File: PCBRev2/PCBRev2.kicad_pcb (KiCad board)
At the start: 2 copper layers, 223.5 x 160 mm, 55 parts, among them J1 Conn_02x40_Counter_Clockwise, J3 512964594, J5 Keypad, J6 Conn_02x10_Odd_Even, J7 54-00164, Q1 2N7000, SW1 SW_Push, SW2 SW_Push, SW3 SW_Push, U1 NUCLEO-G0B1RE, U10 BH1750FVI-TR, U11 MCP6002-I_P, U12 DRV8833PWP, U2 LP-MSPM0G3507, U4 SN74AHC14N, U5 LM7805_TO220, U6 TLV1117-33, U7 COM-09032, U8 WST-1205S, U9 AL5809-20QP1-7

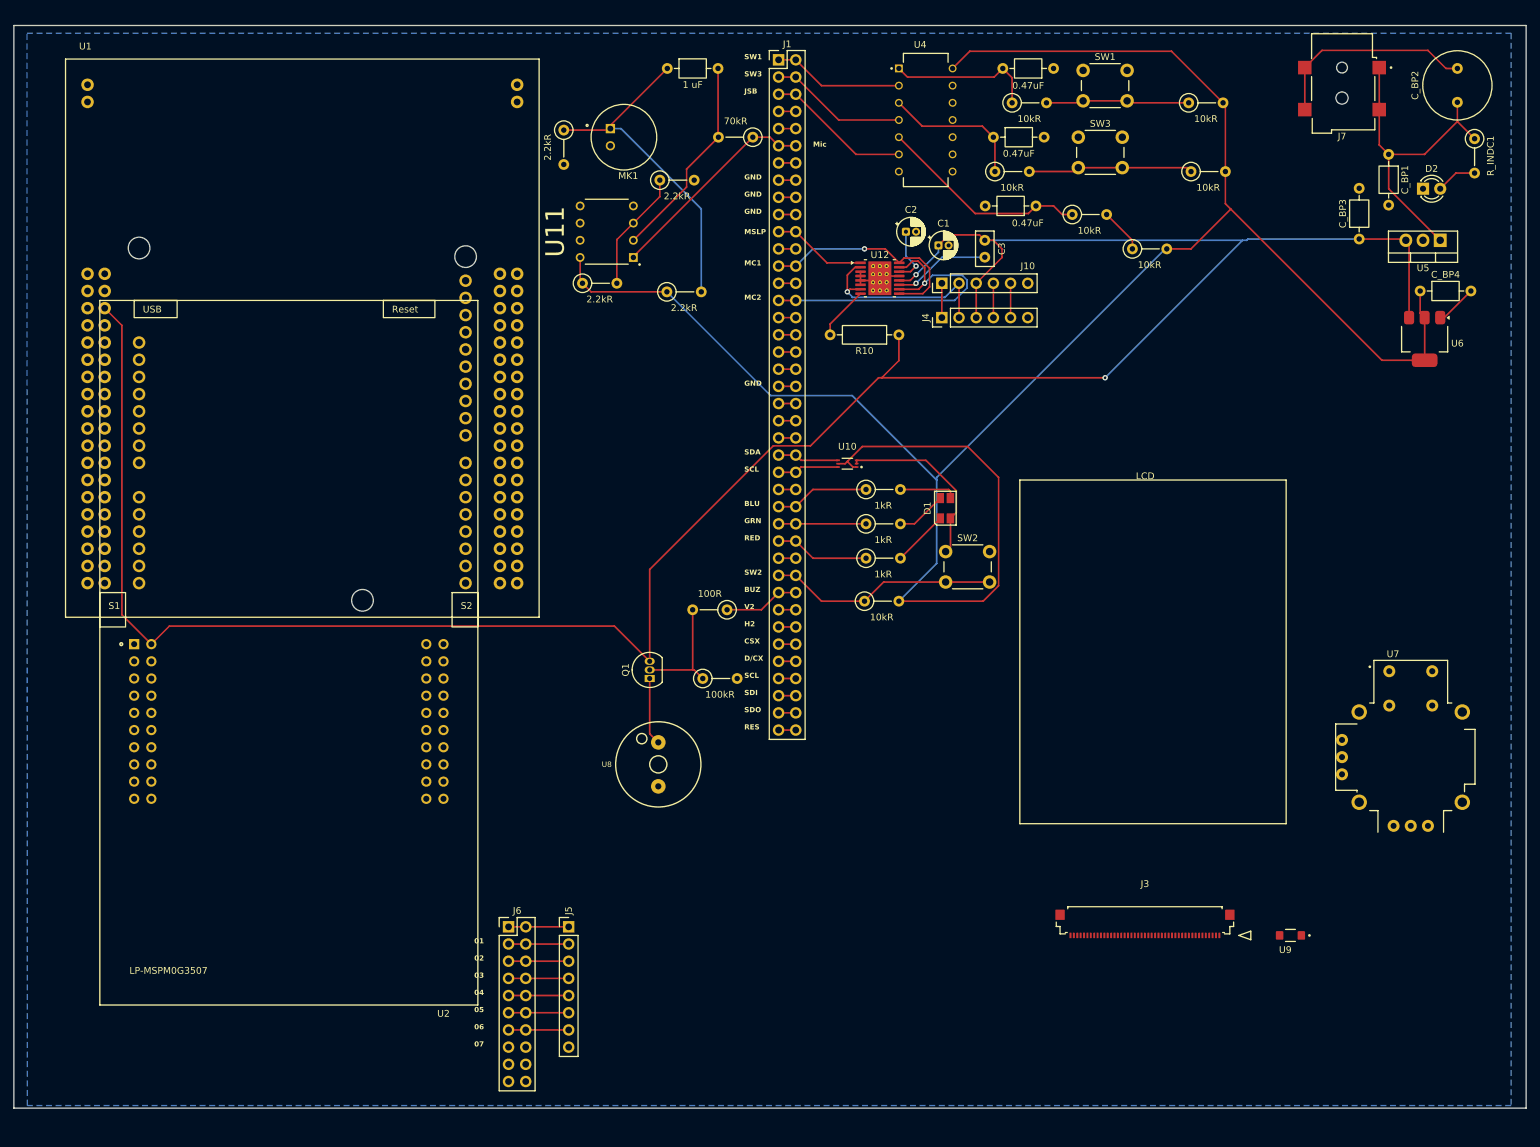
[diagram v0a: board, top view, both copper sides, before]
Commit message: Routing for second revision of the PCB
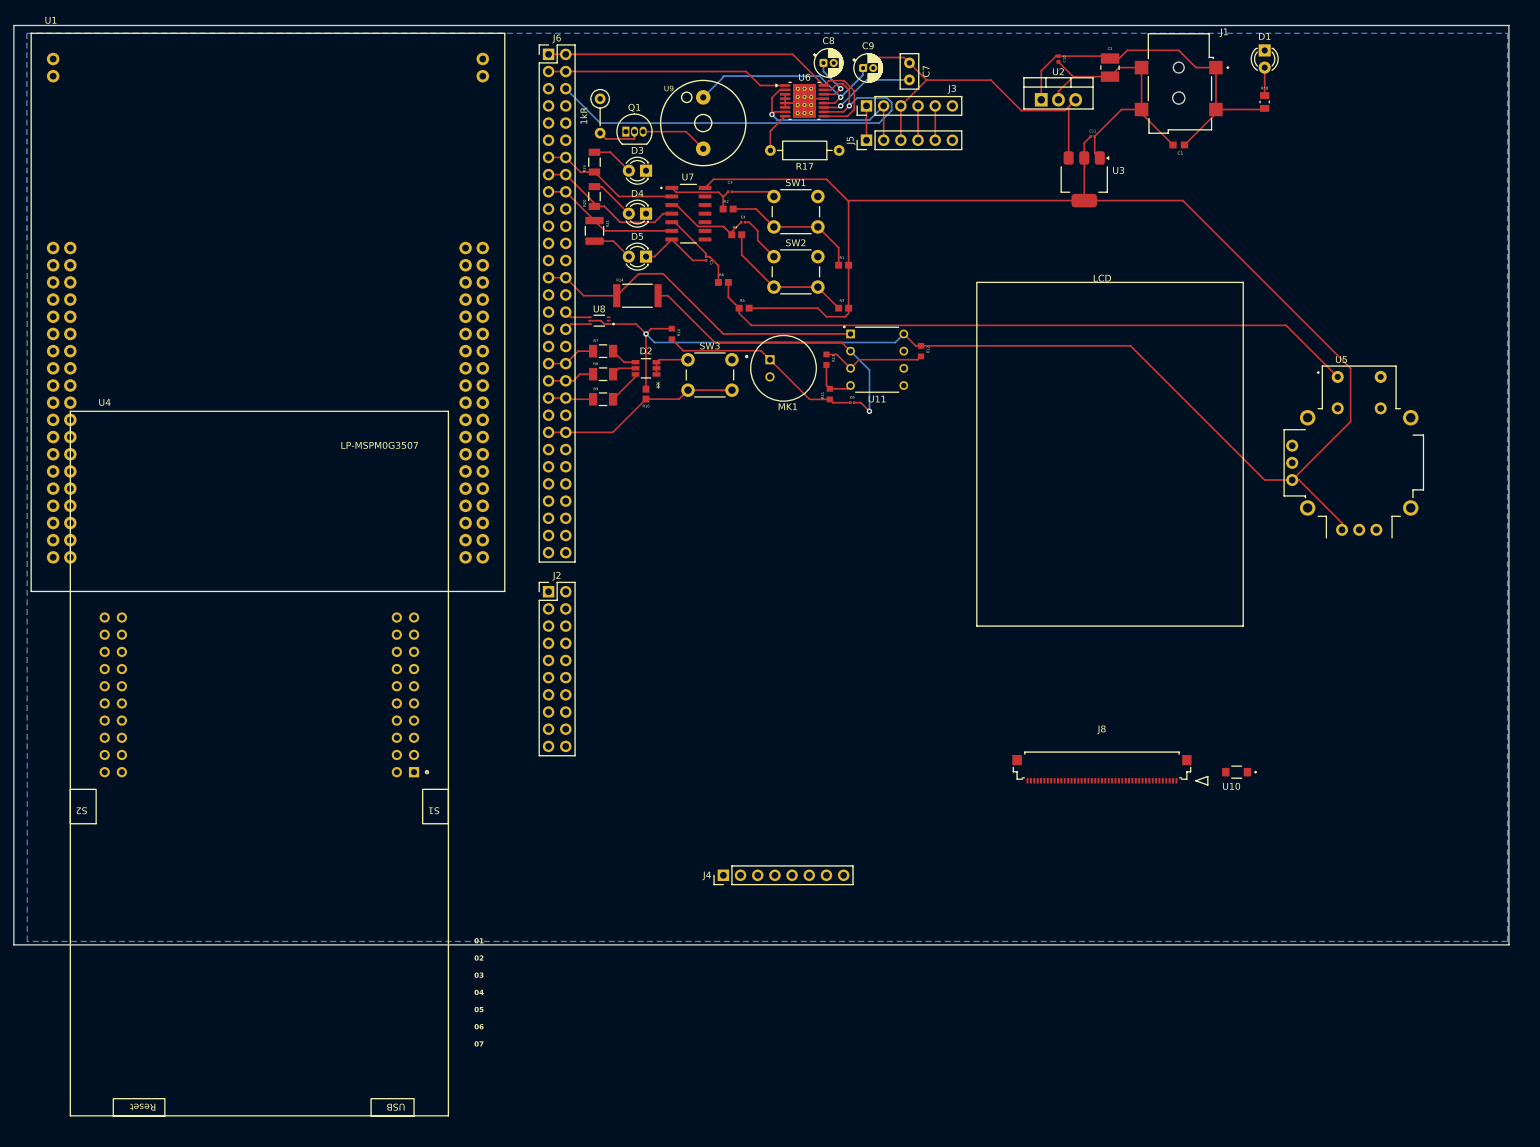
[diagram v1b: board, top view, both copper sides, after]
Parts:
- removed C_BP3, C_BP4: 100 uf, Capacitor_THT:C_Axial_L3.8mm_D2.6mm_P7.50mm_Horizontal
- removed the D1 at (148.4, 82.9)
- removed the J1 at (123.7, 16.6)
- removed R_BUZ2: 100kR, Resistor_THT:R_Axial_DIN0207_L6.3mm_D2.5mm_P5.08mm_Vertical
- removed the U8 at (106.0, 120.8)
- added C10: 0.22uf, GRM155R71C224KA12D022uf.step:CAPC1005X55N, F.Cu at (165.1, 16.5)
- added C11: 1uf, CL03A105KP3NSNC1uf.step:CAPC0603X35N, F.Cu at (170.2, 27.9)
- added D2: AAAF3529LSEEZGKQBKS, footprints:LED_AAAF3529LSEEZGKQBKS_KNB, F.Cu at (104.1, 62.2)
- added D3: LED, LED_THT:LED_D3.0mm_FlatTop, F.Cu at (104.1, 33.0)
- added D4: LED, LED_THT:LED_D3.0mm_FlatTop, F.Cu at (104.1, 39.4)
- added D5: LED, LED_THT:LED_D3.0mm_FlatTop, F.Cu at (104.1, 45.7)
- added J6: Conn_02x30_Odd_Even, Connector_PinHeader_2.54mm:PinHeader_2x30_P2.54mm_Vertical, F.Cu at (89.7, 15.8)
- added R19: 68, CRGCQ1206F68R.step:RESC3115X65N, F.Cu at (96.5, 31.8)
- added R20: 68, CRGCQ1206F68R.step:RESC3115X65N, F.Cu at (96.5, 36.8)
- added R21: 330, CRCW1210330RFKEAHP.step:RESC3225X70N, F.Cu at (96.5, 41.9)
- added U9: WST-1205S, WST-1205S.step:WST-1205S, F.Cu at (112.6, 26.0)
- C1: renamed from C_BP1; value 0.1 uf -> 0.1uf; footprint Capacitor_THT:C_Axial_L3.8mm_D2.6mm_P7.50mm_Horizontal -> C01UF.step:CAPC1608X90
- C2: renamed from C_BP2; value 47 uf -> 47uf; footprint Capacitor_THT:C_Radial_D10.0mm_H20.0mm_P5.00mm -> GRM32EC81C476KE15L.step:CAPC3225X270N
- C3: renamed from CSW1; footprint Capacitor_THT:C_Axial_L3.8mm_D2.6mm_P7.50mm_Horizontal -> GRM033R60J474KE90D.step:CAPC0603X33N
- C4: renamed from CSW3; footprint Capacitor_THT:C_Axial_L3.8mm_D2.6mm_P7.50mm_Horizontal -> GRM033R60J474KE90D.step:CAPC0603X33N
- C5: renamed from CJS1; footprint Capacitor_THT:C_Axial_L3.8mm_D2.6mm_P7.50mm_Horizontal -> GRM033R60J474KE90D.step:CAPC0603X33N
- C6: renamed from C_s2; footprint Capacitor_THT:C_Axial_L3.8mm_D2.6mm_P7.50mm_Horizontal -> CL03A105KP3NSNC1uf.step:CAPC0603X35N
- Q1: value 2N7000 -> 2N4401
- R1: renamed from PullUpResistorSW1; footprint Resistor_THT:R_Axial_DIN0207_L6.3mm_D2.5mm_P5.08mm_Vertical -> RC0603FR_0710KL.step:RESC1607X60N
- R10: renamed from R_SNSA2; footprint Resistor_THT:R_Axial_DIN0207_L6.3mm_D2.5mm_P5.08mm_Vertical -> CRGCQ0603F2K2.step:RESC1608X55N
- R11: renamed from R_SNSA3; footprint Resistor_THT:R_Axial_DIN0207_L6.3mm_D2.5mm_P5.08mm_Vertical -> CRGCQ0603F2K2.step:RESC1608X55N
- R12: renamed from R_SNSA5; footprint Resistor_THT:R_Axial_DIN0207_L6.3mm_D2.5mm_P5.08mm_Vertical -> CRGCQ0603F2K2.step:RESC1608X55N
- R13: renamed from R_SNSA6; footprint Resistor_THT:R_Axial_DIN0207_L6.3mm_D2.5mm_P5.08mm_Vertical -> CRGCQ0603F2K2.step:RESC1608X55N
- R14: renamed from R_SNSA4; value 70kR -> 68k; footprint Resistor_THT:R_Axial_DIN0207_L6.3mm_D2.5mm_P5.08mm_Vertical -> CRGP2512F68K.step:RESC6332X65N
- R15: renamed from R_BUZ1; value 100R -> 1kR
- R16: renamed from PullUpResistor2; footprint Resistor_THT:R_Axial_DIN0207_L6.3mm_D2.5mm_P5.08mm_Vertical -> RC0603FR_0710KL.step:RESC1607X60N
- R18: renamed from R_INDC1; value 5.5k ohm -> 510; footprint Resistor_THT:R_Axial_DIN0207_L6.3mm_D2.5mm_P5.08mm_Vertical -> RMCF0805JT510R510.step:RESC2012X65N
- R2: renamed from RSW1; footprint Resistor_THT:R_Axial_DIN0207_L6.3mm_D2.5mm_P5.08mm_Vertical -> RC0603FR_0710KL.step:RESC1607X60N
- R3: renamed from PullUpResistorSW3; footprint Resistor_THT:R_Axial_DIN0207_L6.3mm_D2.5mm_P5.08mm_Vertical -> RC0603FR_0710KL.step:RESC1607X60N
- R4: renamed from RSW3; footprint Resistor_THT:R_Axial_DIN0207_L6.3mm_D2.5mm_P5.08mm_Vertical -> RC0603FR_0710KL.step:RESC1607X60N
- R5: renamed from PullUpResistorJS1; footprint Resistor_THT:R_Axial_DIN0207_L6.3mm_D2.5mm_P5.08mm_Vertical -> RC0603FR_0710KL.step:RESC1607X60N
- R6: renamed from RJS1; footprint Resistor_THT:R_Axial_DIN0207_L6.3mm_D2.5mm_P5.08mm_Vertical -> RC0603FR_0710KL.step:RESC1607X60N
- R7: renamed from R_COFF2; footprint Resistor_THT:R_Axial_DIN0207_L6.3mm_D2.5mm_P5.08mm_Vertical -> RNCP1206FTD1K00.step:RESC3216X90N
- R8: renamed from R_COFF3; footprint Resistor_THT:R_Axial_DIN0207_L6.3mm_D2.5mm_P5.08mm_Vertical -> RNCP1206FTD1K00.step:RESC3216X90N
- R9: renamed from R_COFF4; footprint Resistor_THT:R_Axial_DIN0207_L6.3mm_D2.5mm_P5.08mm_Vertical -> RNCP1206FTD1K00.step:RESC3216X90N
- U7: renamed from U4; footprint Schmitt:DIP794W45P254L1969H508Q14 -> SN74AHCT14QDRG4Q1.step:SOIC127P600X175-14N
- moved Q1 80.9 mm to (101.2, 27.2), turned to 0 degrees
- moved R15 77.8 mm to (97.4, 22.4), turned to -90 degrees
- moved U2 62.5 mm to (162.6, 22.5), turned to 0 degrees
- moved R5 58.0 mm to (118.6, 53.3)
- moved C6 56.5 mm to (134.6, 67.3)
- moved R1 56.4 mm to (133.3, 47.0)
- moved U3 55.6 mm to (168.9, 34.3)
- moved R11 55.4 mm to (131.3, 66.0), turned to 90 degrees
- moved R3 55.2 mm to (133.3, 53.3)
- moved R6 52.5 mm to (115.6, 49.5)
- moved C2 51.6 mm to (172.7, 17.8), turned to -90 degrees
- moved C3 51.2 mm to (116.6, 36.1)
- moved R12 51.0 mm to (144.8, 59.7), turned to -90 degrees
- moved J2 49.9 mm to (89.7, 95.2)
- moved R7 49.5 mm to (97.8, 59.7)
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- renumbered C3 to C7, C2 to C8, C1 to C9, D2 to D1, J7 to J1, J6 to J2, J10 to J3, J5 to J4, J4 to J5, J3 to J8, R10 to R17, SW3 to SW2, SW2 to SW3, U9 to U10, U5 to U2, U6 to U3, U2 to U4, U7 to U5, U12 to U6, U10 to U8
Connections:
- net /Button No Debouning renamed ButtonNoDebounce
- J8 pad 29: Net-(J1-Pin_77) -> SDO
- J8 pad 30: Net-(J1-Pin_75) -> SDI
- J8 pad 32: Net-(J1-Pin_73) -> SCL
- J8 pad 33: Net-(J1-Pin_71) -> D/CX
- J8 pad 34: Net-(J1-Pin_69) -> CSX
- J8 pad 6: Net-(J1-Pin_79) -> RESX
- Q1 pad 1: Net-(Q1-S) -> GNDREF
- Q1 pad 3: +5V -> Net-(Q1-D)
- R7 pad 1: Net-(J1-Pin_57) -> B
- R8 pad 1: Net-(J1-Pin_55) -> G
- R9 pad 1: Net-(J1-Pin_53) -> R
- U5 pad H2: Net-(J1-Pin_67) -> H
- U5 pad V2: Net-(J1-Pin_65) -> V
- U7 pad 2: Net-(J1-Pin_1) -> SW1
- U7 pad 4: Net-(J1-Pin_3) -> SW2
- U7 pad 6: Net-(J1-Pin_5) -> JSB
- U8 pad 4: Net-(J1-Pin_47) -> SDA
- U8 pad 6: Net-(J1-Pin_49) -> SCLlight
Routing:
- net +5V: track 363.4 -> 87.0 mm, vias 2 -> 1
- net Net-(U5-SEL+): track 6.66 -> 97.6 mm
- net MotorControl1: track 32.8 -> 55.6 mm, vias 1 -> 0
- net MotorControl2: track 47.8 -> 70.2 mm
- net SW2: track 0.00 -> 21.9 mm
- net Motor_Sleep: track 14.0 -> 35.8 mm
- net Net-(J1-Pin_5): track 21.5 -> 0.00 mm
- net JSB: track 0.00 -> 20.6 mm
- net SW1: track 0.00 -> 20.6 mm
- net Net-(J1-Pin_3): track 20.4 -> 0.00 mm
- net Net-(C6-Pad1): track 50.0 -> 30.3 mm
- net Net-(J1-Pin_1): track 19.4 -> 0.00 mm
- net Net-(U7-3A): track 31.3 -> 12.3 mm
- net MicOut: track 32.0 -> 50.8 mm
- net Net-(U11-VINA-): track 30.6 -> 44.7 mm, vias 0 -> 1
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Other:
- board size 223.5 x 160 mm -> 221 x 135.9 mm
- board text removed: "BLU"
- board text removed: "BUZ"
- board text removed: "CSX"
- board text removed: "D/CX"
- board text removed: "GND"
- board text removed: "GRN"
- board text removed: "H2"
- board text removed: "JSB"
- board text removed: "MC1"
- board text removed: "MC2"
- board text removed: "MSLP"
- board text removed: "Mic"
- board text removed: "RED"
- board text removed: "RES"
- board text removed: "SCL"
- board text removed: "SDA"
- board text removed: "SDI"
- board text removed: "SDO"
- board text removed: "SW1"
- board text removed: "SW2"
- board text removed: "SW3"
- board text removed: "V2"

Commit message: Updated routing and footprints for 2nd PCB revision
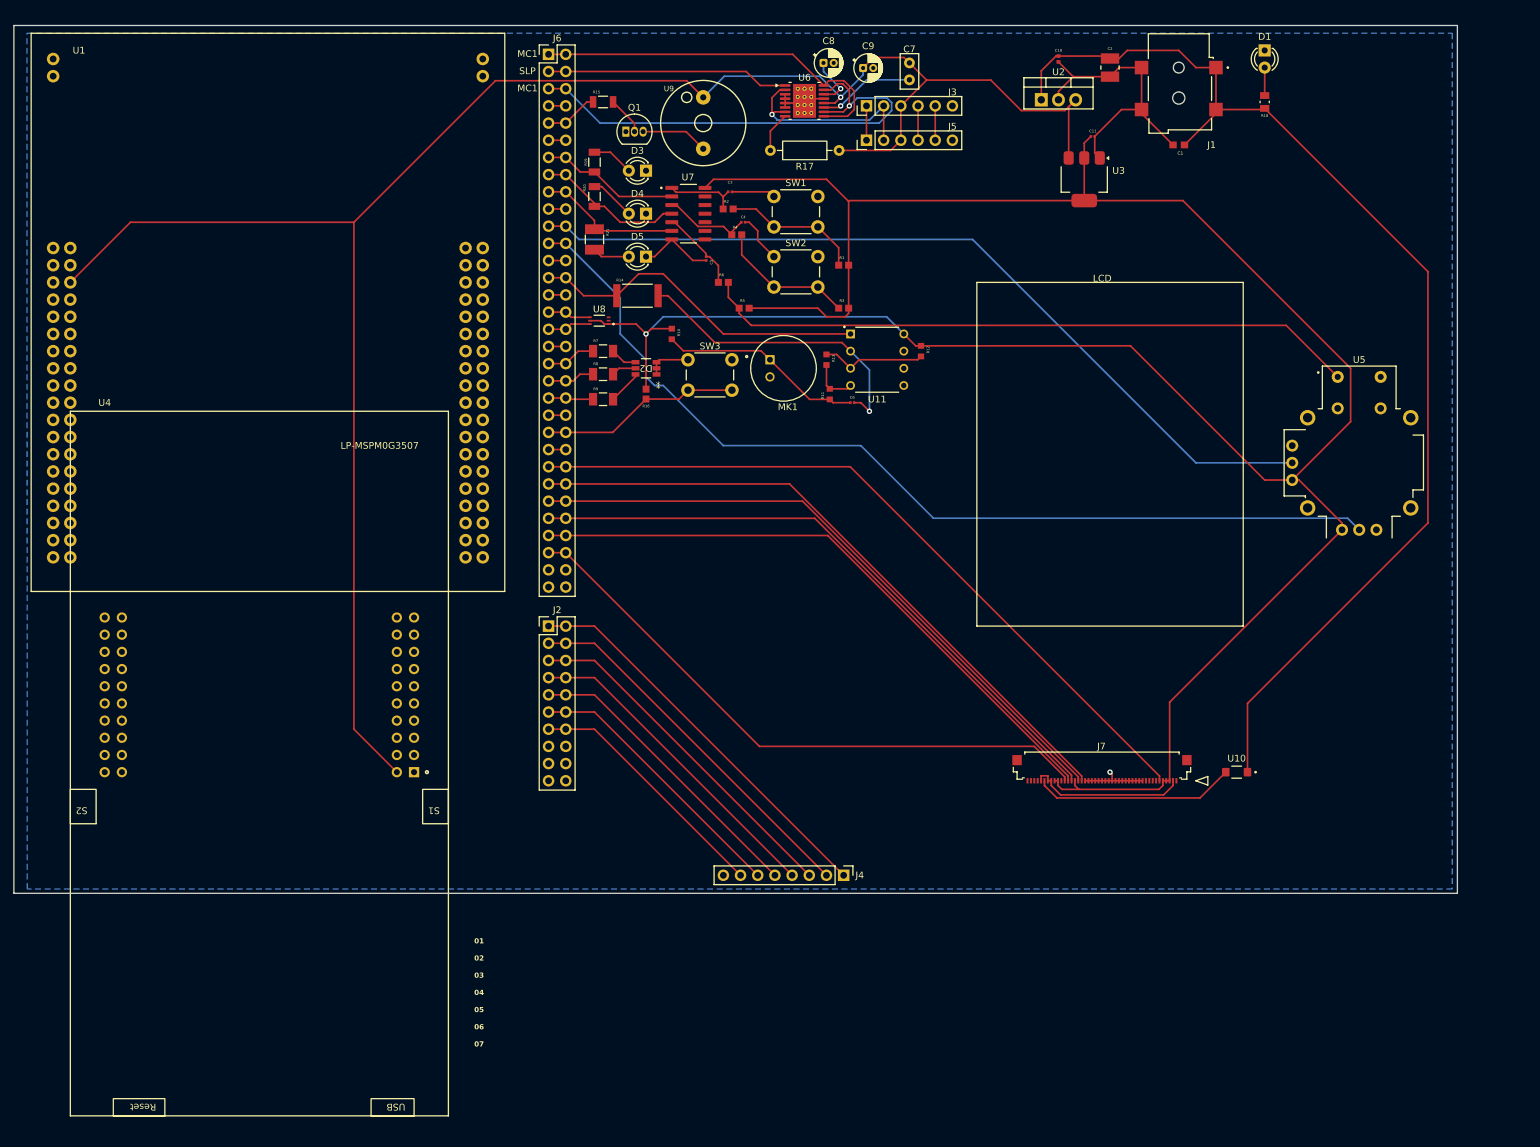
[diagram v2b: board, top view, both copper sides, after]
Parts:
- J6: footprint Connector_PinHeader_2.54mm:PinHeader_2x30_P2.54mm_Vertical -> Connector_PinHeader_2.54mm:PinHeader_2x32_P2.54mm_Vertical
- R15: value 1kR -> 620; footprint Resistor_THT:R_Axial_DIN0207_L6.3mm_D2.5mm_P5.08mm_Vertical -> RC1206JR_07620RL.step:RESC3116X65N
- moved J4 17.8 mm to (133.3, 137.2), turned to -90 degrees
- moved J2 5.08 mm to (89.7, 100.3)
- moved R21 1.27 mm to (96.5, 43.2)
- moved R15 0.64 mm to (97.8, 22.9), turned to 0 degrees
- renumbered J8 to J7
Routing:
- net +5V: track 87.0 -> 287.5 mm
- net H: track 0.00 -> 142.0 mm
- net V: track 0.00 -> 124.4 mm
- net +12V: track 53.3 -> 172.5 mm
- net RESX: track 0.00 -> 109.9 mm
- net SDO: track 0.00 -> 97.4 mm
- net SDI: track 0.00 -> 95.7 mm
- net SCL: track 0.00 -> 93.9 mm
- net D/CX: track 0.00 -> 92.2 mm
- net CSX: track 0.00 -> 90.6 mm
- net VDD: track 307.5 -> 376.6 mm
- net Net-(J2-Pin_1): track 0.00 -> 58.9 mm
- net Net-(J2-Pin_3): track 0.00 -> 55.3 mm
- net Net-(J2-Pin_5): track 0.00 -> 51.7 mm
- net Net-(J2-Pin_7): track 0.00 -> 48.1 mm
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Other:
- board size 221 x 135.9 mm -> 213.4 x 128.3 mm
- board text added: "MC1"
- board text added: "SLP"

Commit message: Added silkscreen references
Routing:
- net GNDREF: track 128.4 -> 132.8 mm, vias 1 -> 2
- net V: track 124.4 -> 125.5 mm
- net H: track 142.0 -> 142.6 mm
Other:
- board text added: "B"
- board text added: "BUZ"
- board text added: "CSX"
- board text added: "D/CX"
- board text added: "G"
- board text added: "H"
- board text added: "JSB"
- board text added: "MIC"
- board text added: "R"
- board text added: "RES"
- board text added: "SCL1"
- board text added: "SCL2"
- board text added: "SDA"
- board text added: "SDI"
- board text added: "SDO"
- board text added: "SW1"
- board text added: "SW2"
- board text added: "SW3"
- board text added: "V"
